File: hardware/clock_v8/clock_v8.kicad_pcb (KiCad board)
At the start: 2 copper layers, 119 x 92 mm, 143 parts, among them J1 RJ45, J10 KH-BNC50-3511, J11 KH-BNC50-3511, J12 Conn_01x06, J13 KH-BNC50-3511, J2 Conn_01x06_Pin, J3 KH-BNC50-3511, J4 USB_C_Receptacle, J5 Conn_01x06_Pin, J6 Conn_01x04_Pin, J8 Conn_01x02, J9 KH-BNC50-3511, Q1 2N7002, Q10 2N7002, Q9 2N7002, U1 ADA4807-1, U10 STM32F405RGTx, U11 AMS1117-3.3, U12 BA50DD0WHFP-TR, U13 M24C02-RMN, U14 CH340C, U15 USBLC6-2P6, U2 SN74LVC1G14DBV, U3 SN74LVC1G14DBV, U4 ADA4807-1, U5 ADA4807-1, U6 TLV3603DCKR, U7 SN74LVC1G14DBV, U8 TLV3603DCKR, U9 L78L05_SOT89, Y1 AOCJY4A-10.000MHZ-SW, Y2 16MHz

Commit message: clean up clock
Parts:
- removed TP19: ~, TestPoint:TestPoint_THTPad_D1.5mm_Drill0.7mm
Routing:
- net OSC_ADJ: track 60.2 -> 36.1 mm, vias 3 -> 2
- net GND: track 1263.3 -> 1260.4 mm
- net /USB_RX: track 155.2 -> 154.4 mm
- net /USB_TX: track 137.4 -> 136.6 mm

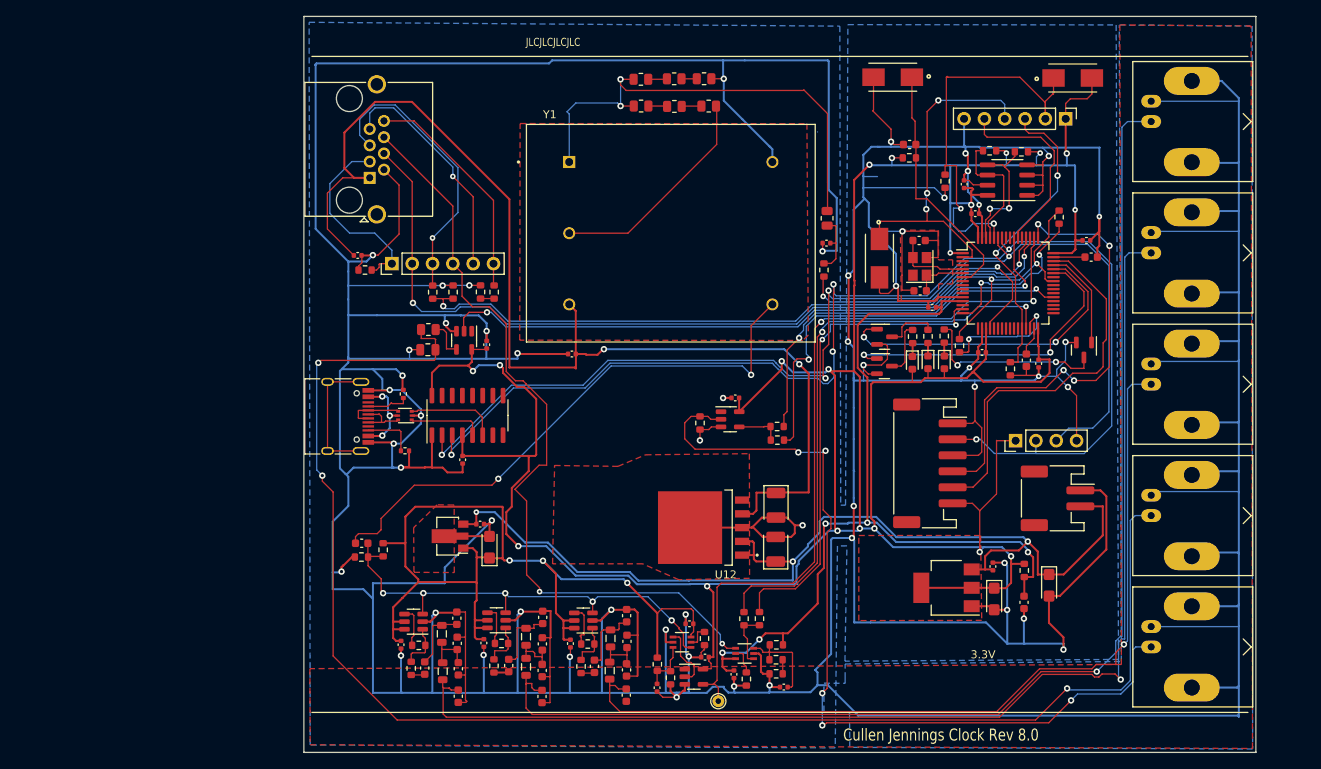
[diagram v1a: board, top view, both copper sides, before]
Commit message: starting 10Mhz Aux clk input
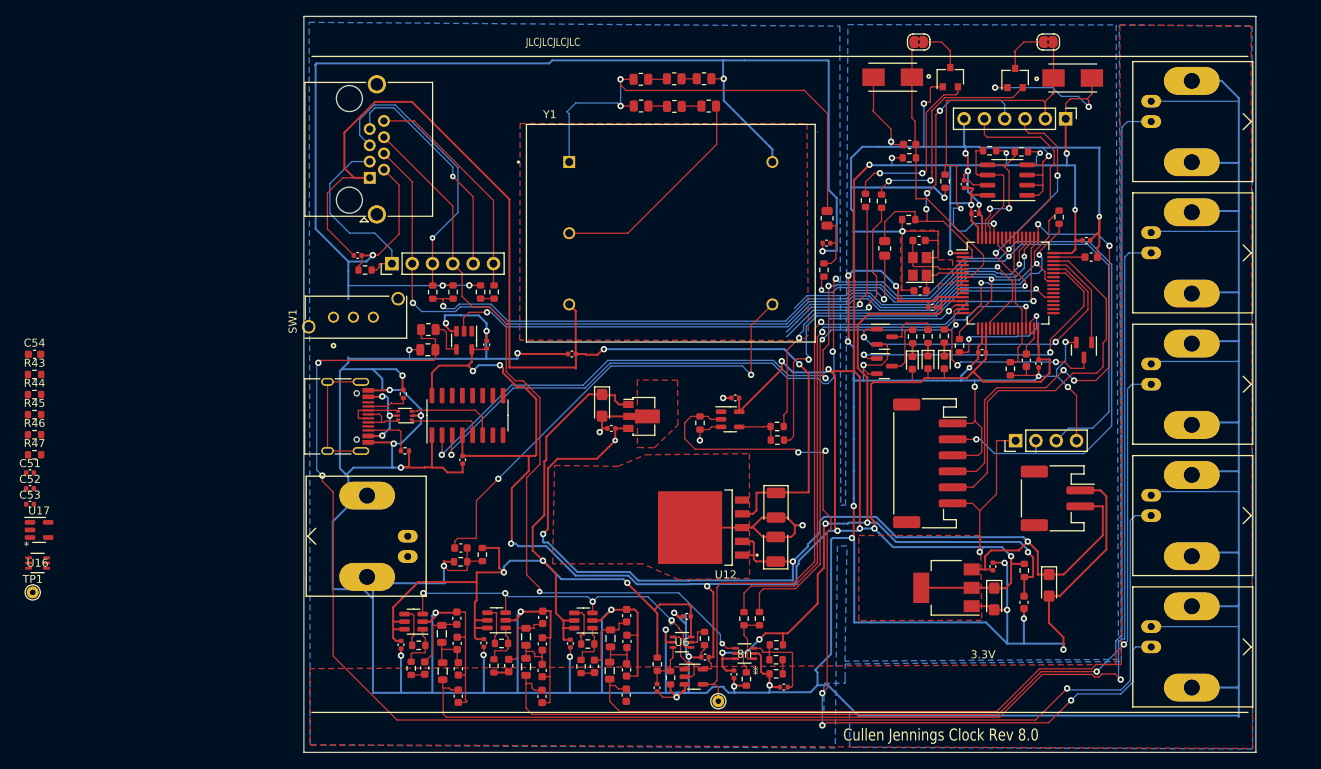
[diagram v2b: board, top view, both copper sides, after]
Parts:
- removed S2: 147873-2, blinky_footprints:SW_147873-2
- added C51: 100n, Capacitor_SMD:C_0402_1005Metric, F.Cu at (60.8, 95.0)
- added C52: 100n, Capacitor_SMD:C_0402_1005Metric, F.Cu at (60.8, 97.0)
- added C53: 100n, Capacitor_SMD:C_0402_1005Metric, F.Cu at (60.8, 99.0)
- added C54: 100n, Capacitor_SMD:C_0603_1608Metric, F.Cu at (61.3, 80.2)
- added J7: KH-BNC50-3511, blinky_footprints:BNC_Amphenol_B6252HB-NPP3G-50_Horizontal-CJ, F.Cu at (105.5, 103.0)
- added JP1: SolderJumper_2_Bridged, Jumper:SolderJumper-2_P1.3mm_Bridged2Bar_RoundedPad1.0x1.5mm, F.Cu at (171.8, 41.2)
- added JP2: SolderJumper_2_Bridged, Jumper:SolderJumper-2_P1.3mm_Bridged2Bar_RoundedPad1.0x1.5mm, F.Cu at (188.1, 41.2)
- added Q2: S8550, Package_TO_SOT_SMD:SC-59, F.Cu at (183.9, 45.7)
- added Q3: S8050, Package_TO_SOT_SMD:SC-59, F.Cu at (175.8, 45.6)
- added R39: 200R, Resistor_SMD:R_0805_2012Metric, F.Cu at (167.6, 67.0)
- added R40: 4K7, Resistor_SMD:R_0603_1608Metric, F.Cu at (170.6, 63.4)
- added R41: 1K0, Resistor_SMD:R_0603_1608Metric, F.Cu at (167.2, 61.1)
- added R42: 1K0, Resistor_SMD:R_0603_1608Metric, F.Cu at (165.2, 61.0)
- added R43: 1K0, Resistor_SMD:R_0603_1608Metric, F.Cu at (61.3, 82.8)
- added R44: 1K0, Resistor_SMD:R_0603_1608Metric, F.Cu at (61.3, 85.3)
- added R45: 130K, Resistor_SMD:R_0603_1608Metric, F.Cu at (61.3, 87.8)
- added R46: 100R, Resistor_SMD:R_0603_1608Metric, F.Cu at (61.3, 90.3)
- added R47: 100R, Resistor_SMD:R_0603_1608Metric, F.Cu at (61.3, 92.8)
- added SW1: LC1258OASP, blinky_footprints:LC1258OASP, F.Cu at (98.7, 75.6)
- added TP1: ~, TestPoint:TestPoint_THTPad_D1.5mm_Drill0.7mm, F.Cu at (61.1, 110.0)
- added U16: TLV3603DCKR, blinky_footprints:SC70_DCK_TEX, F.Cu at (61.7, 106.3)
- added U17: SN74LVC1G14DBV, Package_TO_SOT_SMD:SOT-23-5, F.Cu at (61.9, 102.2)
- moved U9 28.7 mm to (137.5, 88.0), turned to 0 degrees
- moved C34 22.6 mm to (132.3, 86.6), turned to -90 degrees
- moved C33 20.3 mm to (133.4, 89.5), turned to 0 degrees
- moved C24 12.4 mm to (114.6, 104.4)
- moved R16 12.4 mm to (114.6, 106.2)
- moved R15 12.4 mm to (117.3, 105.3)
- moved C25 0.98 mm to (142.9, 113.0)
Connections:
- U10 pad 14: /AUX_CLK -> AUX_CLK
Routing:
- net Net-(Q2-B): track 0.00 -> 28.7 mm, vias 0 -> 2
- net /USB_DTR: track 0.00 -> 25.3 mm, vias 0 -> 1
- net /USB_RTS: track 0.00 -> 23.2 mm, vias 0 -> 1
- net Net-(Q3-B): track 0.00 -> 22.7 mm, vias 0 -> 2
- net Net-(R39-Pad1): track 0.00 -> 18.1 mm, vias 0 -> 1
- net AUX_CLK: track 0.00 -> 17.3 mm, vias 0 -> 1
- net +3.3V: track 409.2 -> 424.4 mm, vias 19 -> 21
- net /10Mhz2.5V: track 58.1 -> 44.2 mm, vias 5 -> 4
- net /OCXO_OUT: track 70.3 -> 60.1 mm
- net +6V: track 124.1 -> 133.5 mm, vias 3 -> 4
- net Net-(JP2-B): track 0.00 -> 6.24 mm
- net Net-(JP1-B): track 0.00 -> 5.86 mm
- net /NRST: track 31.2 -> 35.7 mm
- net GND: track 1260.4 -> 1256.2 mm, vias 54 -> 55
- net /GPS_EXT_PPS: track 98.5 -> 96.0 mm
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
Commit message: rough routing for clock v8 done
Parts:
- moved TP1 65.0 mm to (123.4, 91.6)
- moved R45 59.4 mm to (116.5, 109.9), turned to -90 degrees
- moved C52 59.3 mm to (119.1, 107.7), turned to 90 degrees
- moved U17 57.4 mm to (119.3, 100.3), turned to 90 degrees
- moved R44 57.0 mm to (113.1, 109.1), turned to -90 degrees
- moved R43 56.3 mm to (112.4, 106.5)
- moved C53 56.2 mm to (116.9, 97.1), turned to 180 degrees
- moved C54 55.9 mm to (112.4, 103.1)
- moved C51 55.7 mm to (114.8, 108.6), turned to -90 degrees
- moved U16 55.2 mm to (117.0, 106.3), turned to -90 degrees
- moved R47 54.6 mm to (114.9, 103.6), turned to 90 degrees
- moved R46 53.1 mm to (112.4, 104.8)
- moved R15 21.5 mm to (128.9, 87.2)
- moved R16 21.5 mm to (126.2, 88.1)
- moved C24 21.5 mm to (126.2, 86.4)
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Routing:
- net GND: track 1256.2 -> 1335.4 mm, vias 55 -> 59
- net Net-(R39-Pad1): track 18.1 -> 78.4 mm, vias 1 -> 2
- net AUX_CLK: track 17.3 -> 76.9 mm, vias 1 -> 4
- net /USB_RTS: track 23.2 -> 69.9 mm, vias 1 -> 2
- net /USB_DTR: track 25.3 -> 70.2 mm, vias 1 -> 2
- net /10Mhz2.5V: track 44.2 -> 75.4 mm, vias 4 -> 5
- net /OCXO_OUT: track 60.1 -> 38.4 mm
- net +3.3V: track 424.4 -> 441.3 mm
- net Net-(U16-+): track 0.00 -> 8.57 mm, vias 0 -> 2
- net Net-(U16--): track 0.00 -> 8.27 mm
- net Net-(U16-OUT): track 0.00 -> 5.29 mm
- net +5VA: track 122.8 -> 127.8 mm
- net Net-(J7-In): track 0.00 -> 3.69 mm
- net Net-(J13-In): track 151.0 -> 148.9 mm
- net Net-(U16-LE/HYS): track 0.00 -> 1.79 mm
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
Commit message: clean up routing
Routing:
- net +3.3V: track 441.3 -> 438.6 mm
- net GND: track 1335.4 -> 1337.8 mm
- net +5V: track 146.5 -> 144.9 mm
- net CLK: track 95.5 -> 94.4 mm
- net Net-(J9-In): track 109.2 -> 108.2 mm
- net Net-(J3-In): track 109.5 -> 108.7 mm
- net +6V: track 133.6 -> 132.8 mm
- net Net-(J13-In): track 148.9 -> 148.1 mm
- net AUX_CLK: track 76.9 -> 76.2 mm
- net /Vadj: track 60.6 -> 60.1 mm

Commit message: clean up routing
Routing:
- net +3.3V: track 438.6 -> 434.9 mm
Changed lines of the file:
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@@
   (segment (start 173.026974 83.214572) (end 175.046562 83.214572) (width 0.25) (layer "F.Cu") (net 1))
   (segment (start 149.412747 86.287253) (end 149.412747 87.412747) (width 0.25) (layer "F.Cu") (net 1))
-  (segment (start 161.818189 82.343689) (end 163.774086 82.343689) (width 0.25) (layer "F.Cu") (net 1))
   (segment (start 118.35 97.1) (end 117.38 97.1) (width 0.25) (layer "F.Cu") (net 1))
   (segment (start 166.316138 102.009896) (end 166.316138 101.146936) (width 0.25) (layer "F.Cu") (net 1))
@@
   (segment (start 179.936157 83.665263) (end 187.124352 83.665263) (width 0.25) (layer "F.Cu") (net 1))
   (segment (start 182.720196 109.478893) (end 183.395576 108.803513) (width 0.25) (layer "F.Cu") (net 1))
-  (segment (start 160.5745 81.1) (end 161.818189 82.343689) (width 0.25) (layer "F.Cu") (net 1))
   (segment (start 166.162648 83.720798) (end 171.080791 83.720798) (width 0.25) (layer "F.Cu") (net 1))
   (segment (start 149.4 87.4) (end 149.412747 87.412747) (width 0.25) (layer "F.Cu") (net 1))
@@
   (via (at 176.507413 76.564786) (size 0.7) (drill 0.3) (layers "F.Cu" "B.Cu") (net 100))
   (via (at 159.8 79.1) (size 0.7) (drill 0.3) (layers "F.Cu" "B.Cu") (net 100))
-  (segment (start 159.8 79.1) (end 161.5 77.4) (width 0.15) (layer "B.Cu") (net 100))
-  (segment (start 161.5 77.2) (end 175.872199 77.2) (width 0.15) (layer "B.Cu") (net 100))
+  (segment (start 161.7 77.2) (end 175.872199 77.2) (width 0.15) (layer "B.Cu") (net 100))
+  (segment (start 159.8 79.1) (end 161.7 77.2) (width 0.15) (layer "B.Cu") (net 100))
   (segment (start 175.872199 77.2) (end 176.507413 76.564786) (width 0.15) (layer "B.Cu") (net 100))
-  (segment (start 161.5 77.4) (end 161.5 77.2) (width 0.15) (layer "B.Cu") (net 100))
   (segment (start 160.45341 58.778064) (end 160.445715 58.770369) (width 0.15) (layer "F.Cu") (net 102))
   (segment (start 157.5 47.2) (end 157.442048 47.257952) (width 0.15) (layer "F.Cu") (net 102))

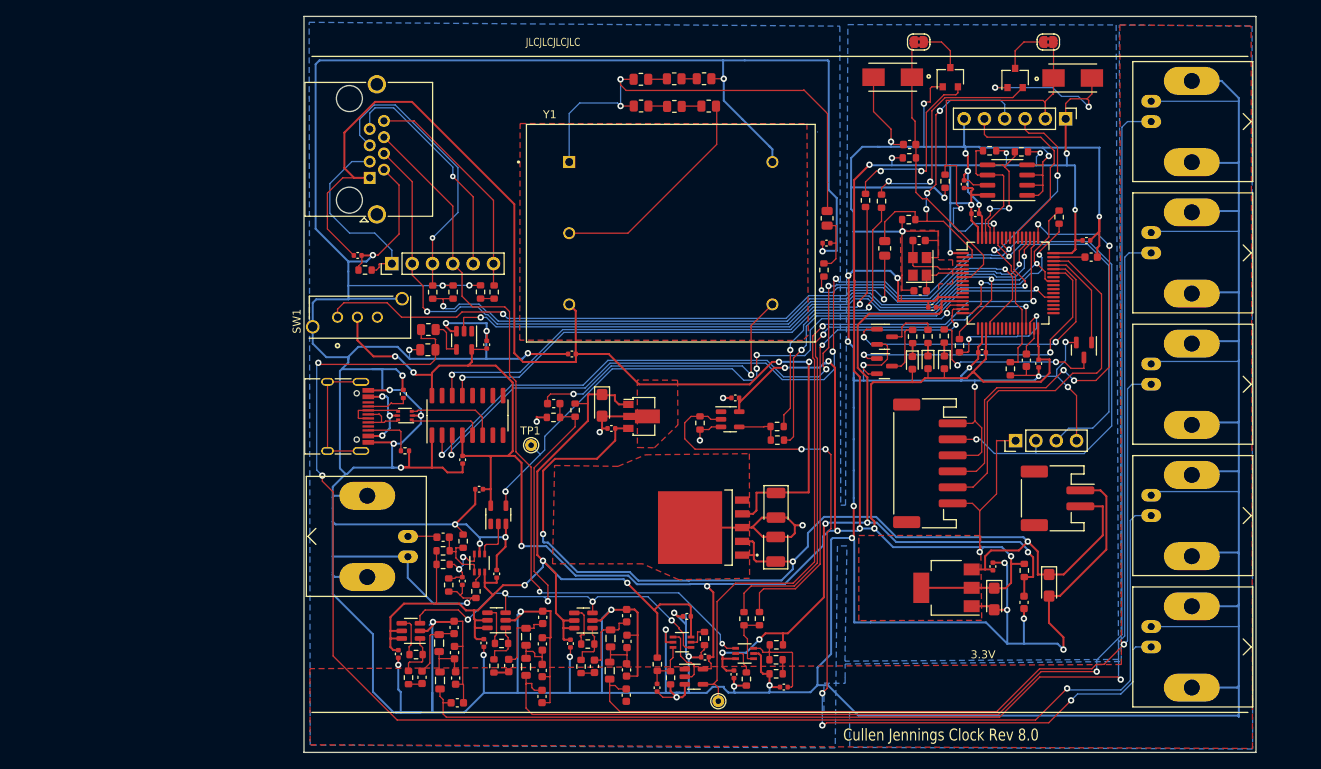
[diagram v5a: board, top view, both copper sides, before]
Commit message: added power connector to clock
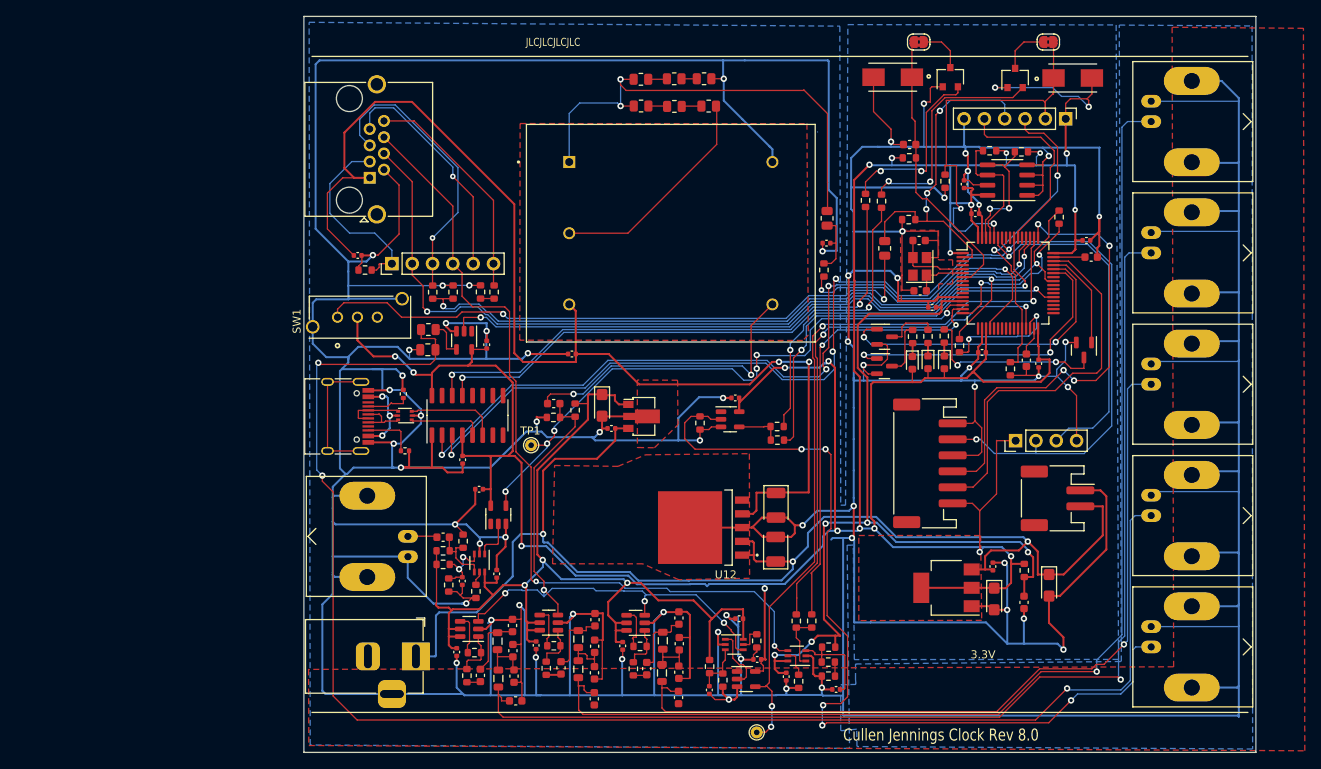
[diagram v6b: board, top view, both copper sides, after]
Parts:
- added J14: DC-063-25A, Connector_BarrelJack:BarrelJack_Horizontal, F.Cu at (109.0, 118.0)
- moved C6 7.30 mm to (121.1, 117.3)
- moved L1 7.30 mm to (119.2, 116.1)
- moved R3 7.30 mm to (115.4, 120.4)
- moved C2 7.30 mm to (114.1, 117.5)
- moved C3 7.30 mm to (117.1, 120.4)
- moved C5 7.30 mm to (121.1, 114.1)
- moved C7 7.30 mm to (121.5, 123.6)
- moved L2 7.30 mm to (119.3, 120.8)
- moved R2 7.30 mm to (116.3, 117.5)
- moved U1 7.30 mm to (115.7, 114.6)
- moved C8 7.30 mm to (121.3, 120.5)
- moved C20 6.54 mm to (141.9, 116.4)
- moved C48 6.54 mm to (161.5, 122.1)
- moved L3 6.54 mm to (129.3, 115.8)
- moved L4 6.54 mm to (129.3, 119.6)
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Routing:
- net GND: track 1337.8 -> 1401.7 mm, vias 59 -> 60
- net +6V: track 132.8 -> 160.5 mm
- net /GPS_EXT_PPS: track 95.2 -> 103.5 mm
- net Net-(J11-In): track 153.9 -> 147.3 mm
- net Net-(J3-In): track 108.7 -> 102.3 mm
- net Net-(J13-In): track 148.1 -> 142.2 mm
- net GPS_PPS: track 71.8 -> 66.2 mm
- net AUX_GPS_PPS: track 60.1 -> 55.4 mm
- net Net-(J9-In): track 108.2 -> 111.5 mm
- net Net-(J10-In): track 186.1 -> 189.0 mm
- net +5VA: track 127.8 -> 130.3 mm
- net CLK: track 94.4 -> 92.9 mm, vias 2 -> 4
- net +3.3VA: track 106.3 -> 105.6 mm
- net AUX_CLK: track 76.2 -> 76.7 mm, vias 4 -> 6
- net /10Mhz2.5V: track 75.4 -> 75.5 mm, vias 5 -> 4

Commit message: clean up symbols
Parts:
- Q2, Q3: footprint Package_TO_SOT_SMD:SC-59 -> Package_TO_SOT_SMD:SOT-23

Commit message: version submitted for build of clock_v8
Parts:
- moved SW1 5.32 mm to (104.5, 76.0), turned to -90 degrees
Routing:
- net Net-(R39-Pad1): track 78.4 -> 72.7 mm
- net GND: track 1401.7 -> 1404.3 mm
- net +3.3V: track 435.1 -> 434.6 mm
